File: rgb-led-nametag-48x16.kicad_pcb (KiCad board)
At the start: 4 copper layers, 84 x 28.8 mm, 138 parts, among them J1 USB_C_Receptacle_USB2.0, J2 TagConnect_TC2030_SWD, Q1 CJ3139K, Q10 CJ3139K, Q11 CJ3139K, Q12 CJ3139K, Q13 CJ3139K, Q14 CJ3139K, Q15 CJ3139K, Q16 CJ3139K, Q2 CJ3139K, Q3 CJ3139K, Q4 CJ3139K, Q5 CJ3139K, Q6 CJ3139K, Q7 CJ3139K, Q8 CJ3139K, Q9 CJ3139K, U1 led-panel-16x16, U10 74HC595, U11 74HC595, U12 74HC595, U13 74HC595, U14 74HC595, U15 74HC595, U16 led-panel-16x16, U17 74HC595, U18 74HC595, U19 74HC595, U2 74HC595, U20 74HC595, U21 74HC595, U22 74HC595, U23 74HC595, U24 ESP32-PICO-D4, U25 STM32F722RETx, U26 SRV05-4, U27 TPS63001, U3 74HC595, U4 74HC595, U5 74HC595, U6 74HC595, U7 74HC595, U8 74HC595, U9 led-panel-16x16

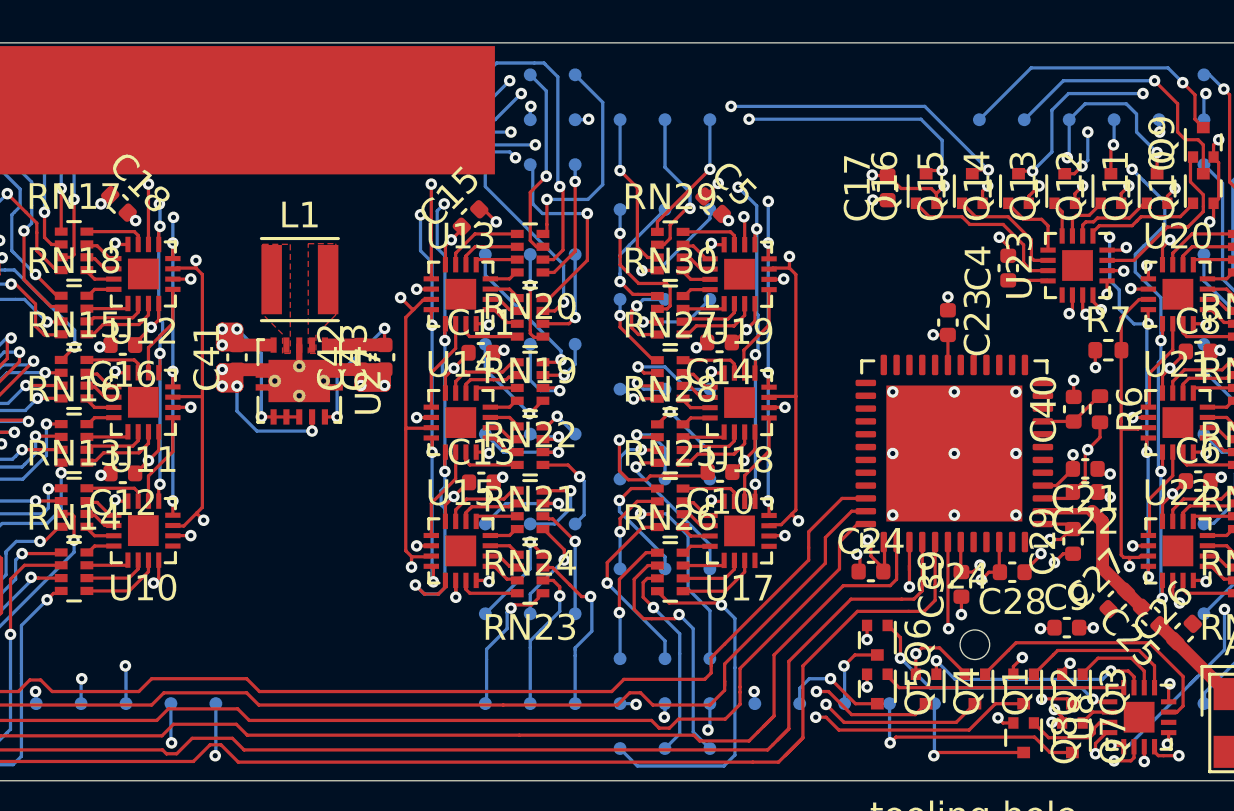
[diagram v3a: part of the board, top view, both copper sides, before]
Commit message: Implement power path
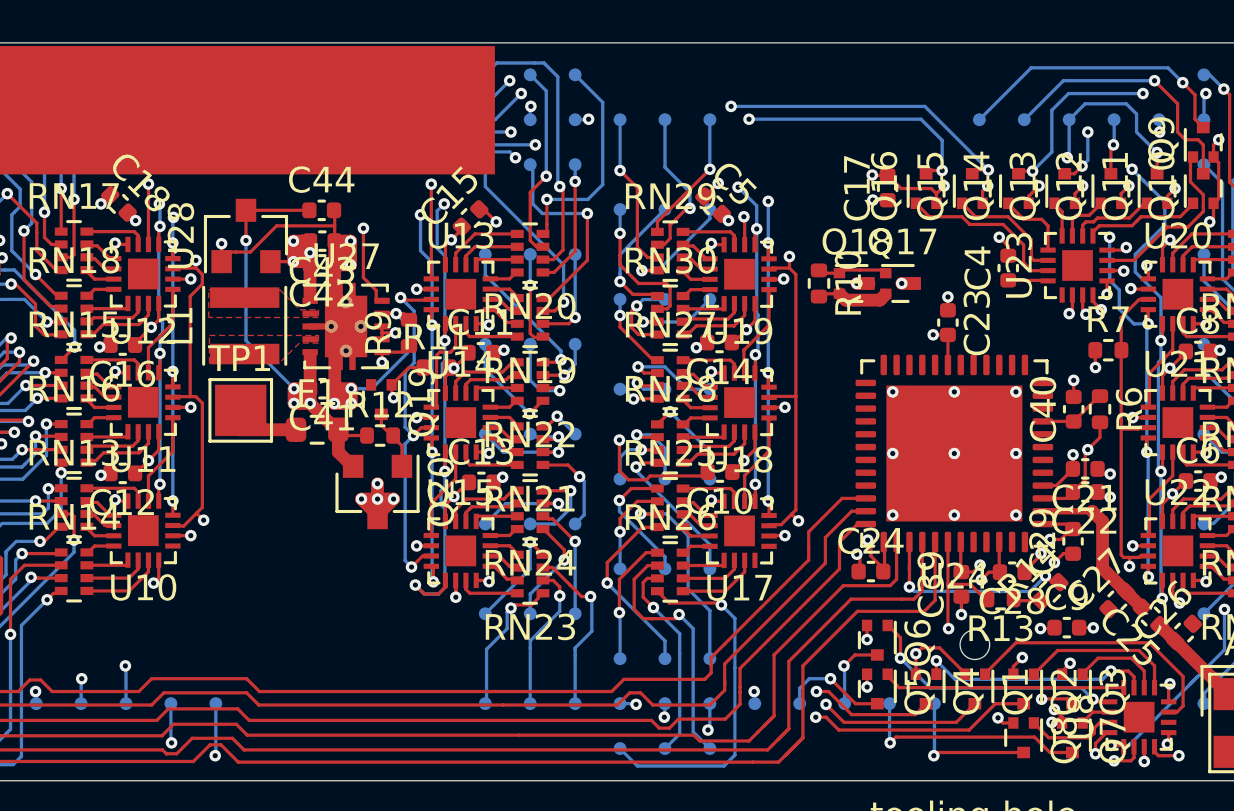
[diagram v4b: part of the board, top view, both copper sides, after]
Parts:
- added C44: 1uF, Capacitor_SMD:C_0402_1005Metric, F.Cu at (136.7, 101.2)
- added F1: 4A, Resistor_SMD:R_0603_1608Metric, F.Cu at (136.5, 109.8)
- added Q17: CJ3139K, Package_TO_SOT_SMD:SOT-723, F.Cu at (159.2, 104.1)
- added Q18: CJ3139K, Package_TO_SOT_SMD:SOT-723, F.Cu at (157.4, 104.1)
- added Q19: 2SK3541, Package_TO_SOT_SMD:SOT-723, F.Cu at (139.0, 108.6)
- added Q20: AO3401A, Package_TO_SOT_SMD:SOT-23, F.Cu at (138.8, 112.2)
- added R10: 100k, Resistor_SMD:R_0402_1005Metric, F.Cu at (156.0, 104.1)
- added R11: 100k, Resistor_SMD:R_0402_1005Metric, F.Cu at (141.1, 107.4)
- added R12: 100k, Resistor_SMD:R_0402_1005Metric, F.Cu at (138.9, 110.0)
- added R13: 5.1k, Resistor_SMD:R_0402_1005Metric, F.Cu at (163.1, 116.4)
- added R14: 5.1k, Resistor_SMD:R_0402_1005Metric, F.Cu at (165.0, 116.1)
- added R9: 10k, Resistor_SMD:R_0402_1005Metric, F.Cu at (140.1, 106.0)
- added TP1: BAT+, TestPoint:TestPoint_Pad_2.0x2.0mm, F.Cu at (133.5, 109.0)
- added U28: XC6206P332MR, Package_TO_SOT_SMD:SOT-23, F.Cu at (133.7, 102.2)
- moved C43 5.13 mm to (136.7, 102.5), turned to 180 degrees
- moved C42 3.90 mm to (136.7, 103.4), turned to 180 degrees
- moved C41 3.55 mm to (136.7, 108.2), turned to 180 degrees
- moved L1 2.80 mm to (133.7, 105.8), turned to 90 degrees
- moved U27 2.80 mm to (137.6, 105.8), turned to 0 degrees
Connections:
- C41 pad 2: Net-(C41-Pad2) -> /VBAT+
- C42 pad 2: Net-(C42-Pad2) -> +3V3
- C43 pad 2: Net-(C42-Pad2) -> +3V3
- U24 pad 39: /Sheet620161B9/SCL -> /SCL
- U24 pad 42: /Sheet620161B9/SDA -> /SDA
- U27 pad 1: Net-(C42-Pad2) -> +3V3
- U27 pad 10: Net-(C42-Pad2) -> +3V3
- U27 pad 5: Net-(C41-Pad2) -> /VBAT+
- U27 pad 6: Net-(C41-Pad2) -> /PWR_EN
- U27 pad 7: Net-(C41-Pad2) -> /VBAT+
- U27 pad 8: Net-(C41-Pad2) -> /VBAT+
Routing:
- net /SCL: track 0.00 -> 62.1 mm, vias 0 -> 2
- net /SDA: track 0.00 -> 59.7 mm, vias 0 -> 1
- net /Sheet620161B9/SDA: track 57.9 -> 0.00 mm, vias 1 -> 0
- net /Sheet620161B9/SCL: track 55.9 -> 0.00 mm, vias 1 -> 0
- net /VBAT+: track 0.00 -> 25.6 mm, vias 0 -> 5
- net +3V3: track 14.2 -> 32.8 mm, vias 2 -> 6
- net Net-(C41-Pad2): track 10.4 -> 0.00 mm, vias 4 -> 0
- net Net-(C42-Pad2): track 9.84 -> 0.00 mm, vias 2 -> 0
- net GND: track 89.7 -> 97.2 mm, vias 51 -> 52
- net /Sheet620161B9/3V3: track 37.0 -> 41.9 mm, vias 7 -> 9
- net VBUS: track 56.9 -> 61.3 mm, vias 76 -> 80
- net Net-(Q17-Pad1): track 0.00 -> 2.67 mm
- net Net-(Q19-Pad3): track 0.00 -> 2.38 mm
- net Net-(F1-Pad1): track 0.00 -> 2.27 mm
- net Net-(Q19-Pad1): track 0.00 -> 2.05 mm, vias 0 -> 1
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
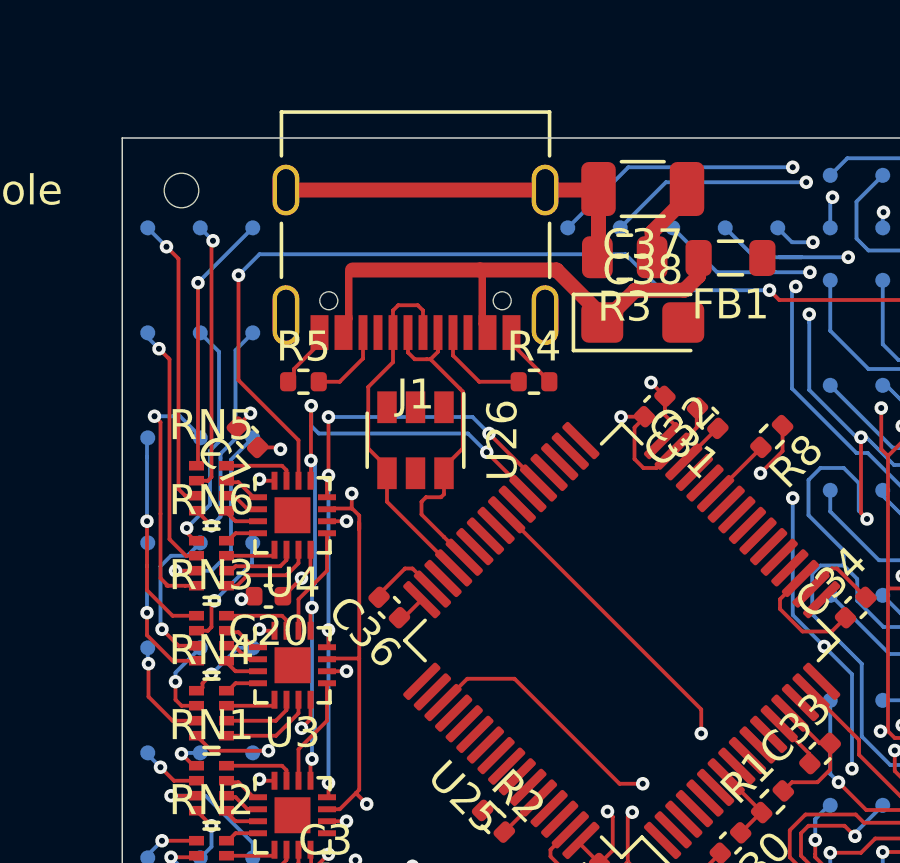
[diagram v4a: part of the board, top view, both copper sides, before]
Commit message: Connect SWD to USB type C SBU
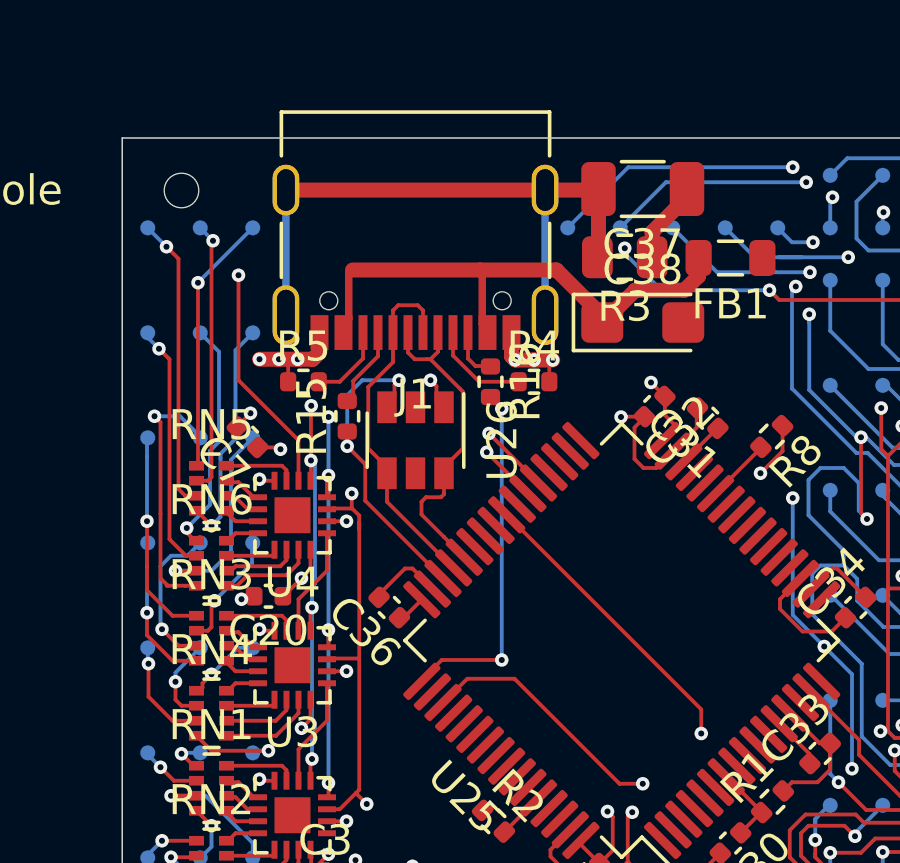
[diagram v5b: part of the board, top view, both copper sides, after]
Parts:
- added R15: 470R, Resistor_SMD:R_0402_1005Metric, F.Cu at (98.9, 104.0)
- added R16: 470R, Resistor_SMD:R_0402_1005Metric, F.Cu at (103.7, 102.8)
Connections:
- U25 pad 46: Net-(U25-Pad46) -> /SWDIO
- U25 pad 49: Net-(U25-Pad49) -> /SWCLK
- U26 pad 1: Net-(U26-Pad1) -> /SWCLK
- U26 pad 3: Net-(U26-Pad3) -> /SWDIO
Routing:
- net /SWCLK: track 0.00 -> 15.5 mm, vias 0 -> 3
- net /SWDIO: track 0.00 -> 10.9 mm, vias 0 -> 2
- net Net-(C37-Pad2): track 12.8 -> 21.4 mm
- net GND: track 97.2 -> 100.4 mm, vias 52 -> 58
- net Net-(J1-PadA8): track 0.00 -> 2.63 mm
- net Net-(J1-PadB8): track 0.00 -> 1.77 mm
- net /Panel 1/sheet61A6C351/SIN: track 34.8 -> 35.3 mm, vias 2 -> 3

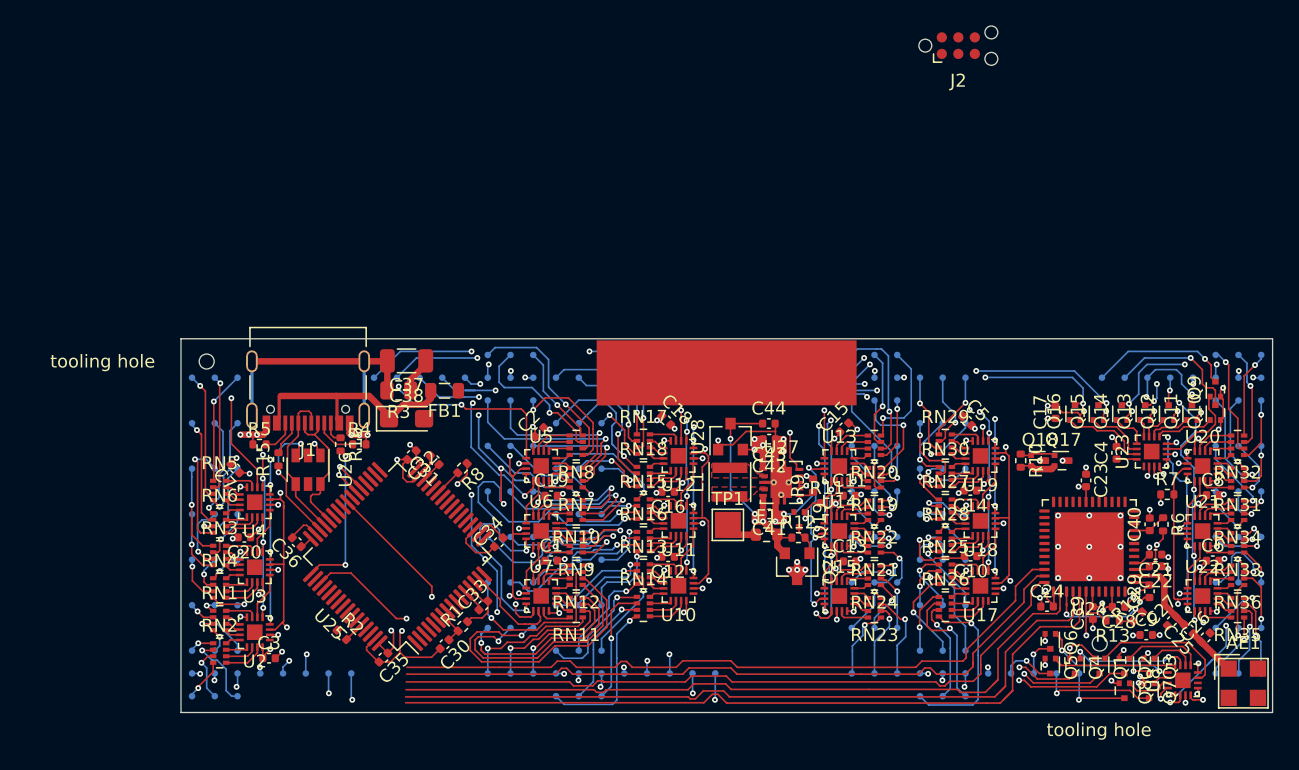
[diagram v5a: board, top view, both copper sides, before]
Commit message: Wire column mux SPI
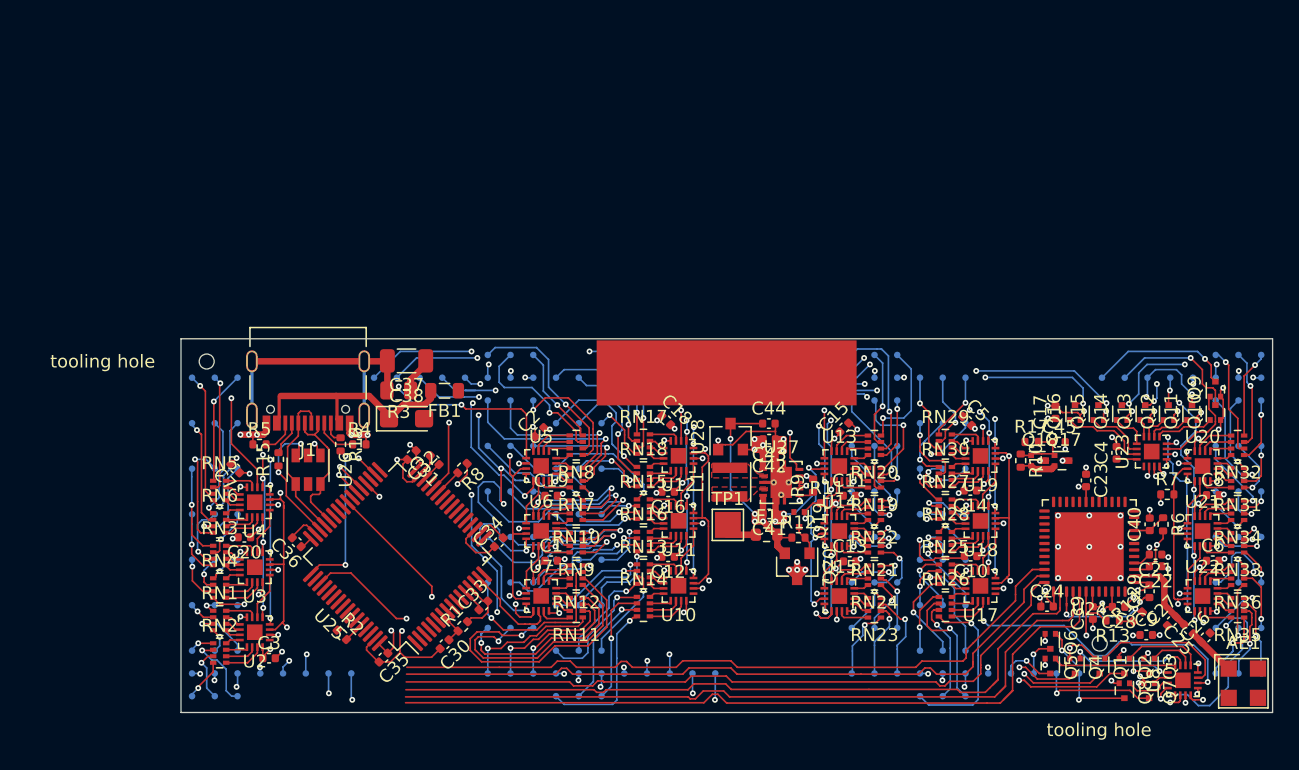
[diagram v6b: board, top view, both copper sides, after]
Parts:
- removed J2: TagConnect_TC2030_SWD, Connector:Tag-Connect_TC2030-IDC-NL_2x03_P1.27mm_Vertical
- added C45: 1uF, Capacitor_SMD:C_0402_1005Metric, F.Cu at (159.0, 102.7)
- added R17: 5.1k, Resistor_SMD:R_0402_1005Metric, F.Cu at (156.9, 102.7)
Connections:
- net Net-(Q19-Pad1) renamed /VBUS_EN
- U26 pad 2: Net-(U26-Pad2) -> GND
- U26 pad 5: Net-(U26-Pad5) -> +5V
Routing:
- net /SPI2_MOSI: track 0.00 -> 74.7 mm, vias 0 -> 3
- net /SPI2_CLK: track 16.8 -> 90.4 mm, vias 2 -> 3
- net /ROW_LATCH: track 24.7 -> 92.9 mm, vias 2 -> 3
- net /sheet61C56D2D/SIN: track 25.6 -> 30.7 mm
- net Net-(C45-Pad1): track 2.67 -> 4.78 mm
- net /Sheet620161B9/3V3: track 41.9 -> 43.7 mm
- net /Panel 3/R2: track 5.23 -> 6.13 mm
- net /QSPI_CLK: track 172.7 -> 173.3 mm
- net GND: track 100.4 -> 100.9 mm, vias 58 -> 59

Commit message: Layout remaining busses
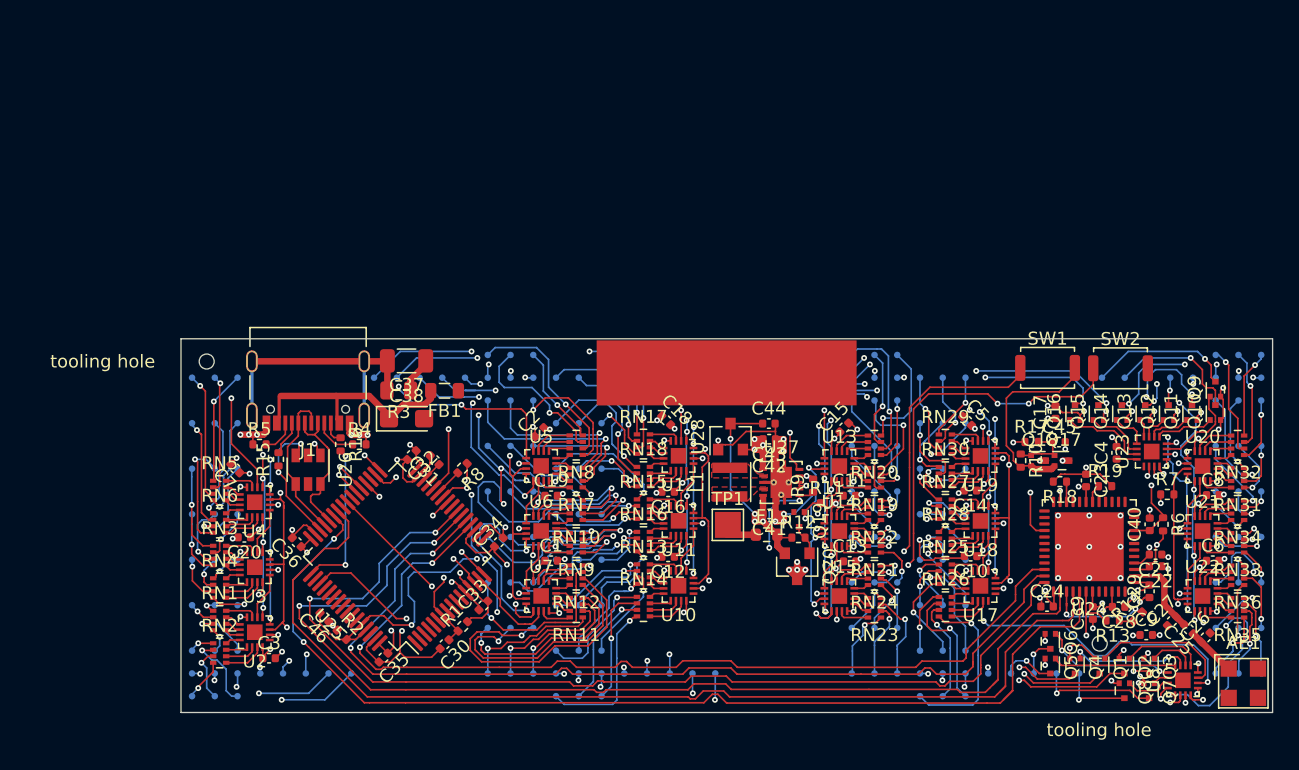
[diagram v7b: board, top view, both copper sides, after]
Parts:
- added C46: 100nF, Capacitor_SMD:C_0402_1005Metric, F.Cu at (102.5, 116.2)
- added R18: 5.1k, Resistor_SMD:R_0402_1005Metric, F.Cu at (159.0, 105.7)
- added R19: 5.1k, Resistor_SMD:R_0402_1005Metric, F.Cu at (162.5, 106.1)
- added SW1: SW_Push, Button_Switch_SMD:SW_Push_SPST_NO_Alps_SKRK, F.Cu at (158.1, 97.0)
- added SW2: SW_Push, Button_Switch_SMD:SW_Push_SPST_NO_Alps_SKRK, F.Cu at (163.7, 97.0)
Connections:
- net /~RTS renamed Net-(U25-Pad62)
- C40 pad 1: /Sheet620161B9/EN -> /EN
- R6 pad 1: /Sheet620161B9/EN -> /EN
- U24 pad 23: /Sheet620161B9/BOOT -> /BOOT
- U24 pad 28: Net-(U24-Pad28) -> /IRQ
- U24 pad 34: /Sheet620161B9/~CS -> /SPI1_~CS
- U24 pad 35: /Sheet620161B9/CLK -> /SPI1_CLK
- U24 pad 36: /Sheet620161B9/MOSI -> /SPI1_MOSI
- U24 pad 38: /Sheet620161B9/MISO -> /SPI1_MISO
- U24 pad 40: /Sheet620161B9/RXD -> /TX
- U24 pad 41: /Sheet620161B9/TXD -> /RX
- U24 pad 9: /Sheet620161B9/EN -> /EN
- U25 pad 14: Net-(U25-Pad14) -> /PWR_EN
- U25 pad 16: Net-(U25-Pad16) -> /IRQ
- U25 pad 25: /IRQ -> /BOOT
- U25 pad 26: Net-(U25-Pad26) -> /EN
- U25 pad 33: /ROW_~RST -> /~ESP_EN
- U25 pad 61: /~DTR -> /DFU
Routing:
- net /SPI1_MISO: track 0.00 -> 84.6 mm, vias 0 -> 2
- net /RX: track 0.00 -> 81.6 mm, vias 0 -> 2
- net /TX: track 0.00 -> 80.8 mm
- net /SPI1_MOSI: track 0.00 -> 80.6 mm, vias 0 -> 2
- net /DFU: track 1.57 -> 80.4 mm, vias 0 -> 3
- net /SPI1_CLK: track 0.00 -> 74.5 mm, vias 0 -> 2
- net /SPI1_~CS: track 0.00 -> 72.8 mm, vias 0 -> 2
- net /~RST: track 2.75 -> 74.4 mm, vias 0 -> 4
- net /EN: track 0.00 -> 66.8 mm, vias 0 -> 2
- net /Sheet620161B9/TXD: track 59.9 -> 0.00 mm
- net /IRQ: track 0.00 -> 59.2 mm, vias 0 -> 2
- net /Sheet620161B9/RXD: track 58.5 -> 0.00 mm
- net /~ESP_EN: track 0.00 -> 57.9 mm, vias 0 -> 2
- net /Sheet620161B9/MISO: track 57.0 -> 0.00 mm
- net /BOOT: track 0.00 -> 56.0 mm, vias 0 -> 2
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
